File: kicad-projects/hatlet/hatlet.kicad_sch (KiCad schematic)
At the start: 40 parts, among them J1 USB Header, J2 SWD, J3 PMOD0, J4 PMOD2, J5 PMOD1, SW1 BOOTSEL, U1 AMS1117-3.3, U2 RP2040, U3 W25Q128JVS, Y1 Crystal 12MHz

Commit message: Finish rev A schematic
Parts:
- added D3: USB, LED_SMD:LED_0201_0603Metric, symbol Device:LED_Small
- added D4: 3V3, LED_SMD:LED_0201_0603Metric, symbol Device:LED_Small
- added J6: UART0, Connector_PinHeader_2.54mm:PinHeader_1x03_P2.54mm_Vertical, symbol Connector:Conn_01x03_Pin
- added J7: PMOD3, pmod:PMOD_PinSocket_2x06_P2.54mm_Horizontal, symbol pmod:PMOD_Host_Conn_02x06
- added R8, R9: 1k, Resistor_SMD:R_0603_1608Metric, symbol Device:R_Small
- SW1: lcsc (none) -> https://www.lcsc.com/product-detail/Tactile-Switches_G-Swit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
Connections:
- net +3V3: now also D4.2 (A), J7.12 (VCC), J7.6 (VCC); no longer U1.2 (VO)
- net GND: now also J1.1 (A0), J1.2 (A1), J1.7 (B0), J1.8 (B1), J6.3 (Pin_3), J7.11 (GND), J7.5 (GND), R8.2, R9.2
- net I2C0_SCL: now also J3.3 (A2); no longer J3.4 (A3)
- net I2C0_SDA: now also J3.4 (A3); no longer J3.3 (A2)
- net I2C1_SCL: now also J3.9 (B2); no longer J3.10 (B3)
- net I2C1_SDA: now also J3.10 (B3); no longer J3.9 (B2)
- net VBUS: now also D3.2 (A)
- net UART0_RX: now reaches J4.9 (B2)
- net UART0_RX: now also U2.28 (GPIO17), J6.2 (Pin_2)
- net UART0_TX: now reaches U2.27 (GPIO16)
- net UART0_TX: now also J4.8 (B1), J6.1 (Pin_1)
- net GPIO24: now reaches U2.36 (GPIO24)
- net GPIO24: now also J7.3 (A2)
- net GPIO25: now reaches U2.37 (GPIO25)
- net GPIO25: now also J7.4 (A3)
- net GPIO26: now reaches U2.38 (GPIO26_ADC0)
- net GPIO26: now also J7.7 (B0)
- net GPIO27: now reaches U2.39 (GPIO27_ADC1)
- net GPIO27: now also J7.8 (B1)
- net GPIO28: now reaches U2.40 (GPIO28_ADC2)
- net GPIO28: now also J7.9 (B2)
- net GPIO29: now reaches U2.41 (GPIO29_ADC3)
- net GPIO29: now also J7.10 (B3)
- net QSPI_CS renamed QSPI_CSn
- net SPI0_INT: no longer names the net of J4.7 (B0)
- net SPI0_INT: no longer U2.34 (GPIO22)
- net SPI0_RESET renamed GPIO23
- net GPIO23: now also J7.2 (A1); no longer J4.8 (B1)
- new net: D3.1 (K), R8.1
- new net: D4.1 (K), R9.1
- new net GPIO22: J7.1 (A0), U2.34 (GPIO22)
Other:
- note added: "-- top row (SPI0) -- 1 SPI0 ~{CS} (GPIO21) 2 SPI0 MOSI (GPIO19) 3 SPI0 MISO (GPIO20) 4 SPI0 SCK (GPIO18) 5 GND 6 VCC -- bottom row (UART0) -- 7 NC 8 UART0 TX (Host -> PMOD) (GPIO16) 9 UART0 RX (Host <- PMOD) (GPIO17) 10 NC 11 GND 12 VCC"
- note added: "-- top row -- 1 GPIO22 2 GPIO23 3 GPIO24 4 GPIO25 5 GND 6 VCC -- bottom row -- 7 GPIO26 8 GPIO27 9 GPIO28 10 GPIO29 11 GND 12 VCC"
- note added: "-- top row -- 1 I2C0 ~{INT} (GPIO2) 2 I2C0 RESET (GPIO3) 3 I2C0 SCL (GPIO5) 4 I2C0 SDA (GPIO4) 5 GND 6 VCC -- bottom row -- 7 I2C1 ~{INT} (GPIO6) 8 I2C1 RESET (GPIO7) 9 I2C1 SCL (GPIO9) 10 I2C1 SDA (GPIO8) 11 GND 12 VCC"
- note added: "-- top row -- 1 SPI1 ~{CS} (GPIO13) 2 SPI1 MOSI (GPIO11) 3 SPI1 MISO (GPIO12) 4 SPI1 SCK (GPIO10) 5 GND 6 VCC -- bottom row -- 7 SPI0 INT (GPIO14) 8 SPI0 RESET (GPIO15) 9 NC 10 NC 11 GND 12 VCC"
- note added: "PMOD1 Pinout (Extended SPI)"
- note added: "PMOD2 Pinout (SPI/UART)"
- note added: "PMOD3 Pinout (GPIO)"
- note added: "Pads for UART header"
- note added: "Power Indicators"
- note added: "SWD rescue port"
- note added: "The RP2040 peripherals can be routed pretty freely across the availble IO. However, when assigning them to PMOD sockets, the pin order of the RP2040 pin mux and the PMOD connector generally don't match."
- note removed: "-- top row -- 1 I2C0 ~{INT} (GPIO2) 2 I2C0 RESET (GPIO3) 3 I2C0 SCL (GPIO4) 4 I2C0 SDA (GPIO5) 5 GND 6 VCC -- bottom row -- 7 I2C1 ~{INT} (GPIO6) 8 I2C1 RESET (GPIO7) 9 I2C1 SCL (GPIO8) 10 I2C1 SDA (GPIO9) 11 GND 12 VCC"
- note removed: "-- top row -- 1 SPI1 ~{CS} (GPIO13) 2 SPI1 MOSI (GPIO11) 3 SPI1 MISO (GPIO12) 4 SPI1 SCK (GPIO10) 5 GND 6 VCC -- bottom row -- 7 SPI0 INT (GPIO14) 8 SPI0 RESET (GPIO15) 9 N/S 10 N/S 11 GND 12 VCC"
- note removed: "Good to have: - LEDs! - SPI PMOD - I2C PMOD - UART PMOD"
- note removed: "PMOD1 Pinout (SPI)"
- note removed: "PMOD2 Pinout (SPI)"
- moved on the sheet: C12, C13, D1, D2, J2, J3, J4, R6, R7, U1

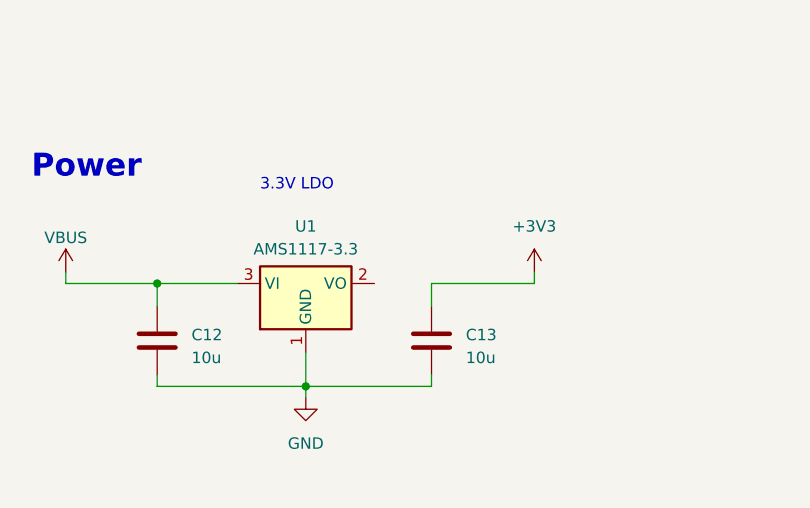
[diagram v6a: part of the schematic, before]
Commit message: Start rev A layout
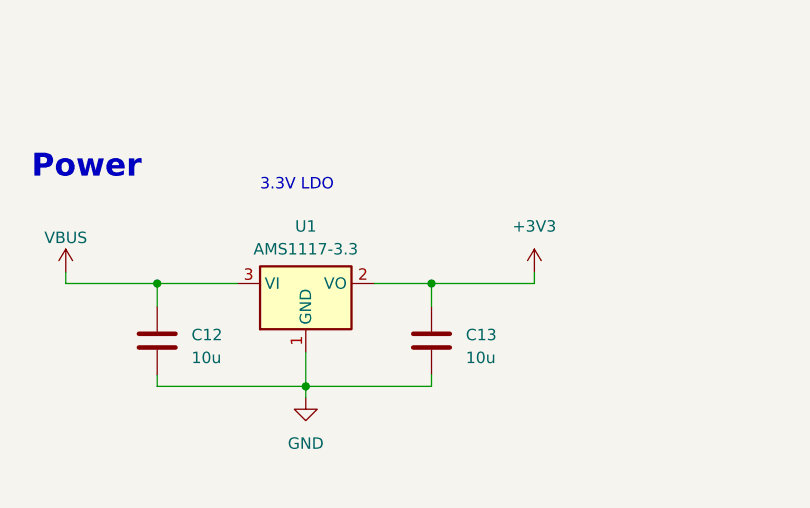
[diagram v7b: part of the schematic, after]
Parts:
- C14, C15, C16: footprint Capacitor_SMD:C_0201_0603Metric -> Capacitor_SMD:C_0603_1608Metric
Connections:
- net +3V3: now also U1.2 (VO)
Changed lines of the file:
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@@
   (junction (at 63.5 209.55) (diameter 0) (color 0 0 0 0)
   )
+  (junction (at 210.82 261.62) (diameter 0) (color 0 0 0 0)
+  )
   (junction (at 71.12 271.78) (diameter 0) (color 0 0 0 0)
   )
@@
     (stroke (width 0) (type default))
   )
+  (wire (pts (xy 204.47 261.62) (xy 210.82 261.62))
+    (stroke (width 0) (type default))
+  )
   (wire (pts (xy 80.01 264.16) (xy 80.01 265.43))
     (stroke (width 0) (type default))
@@
       (effects (font (size 1.27 1.27)) (justify right))
     )
-    (property "Footprint" "Capacitor_SMD:C_0201_0603Metric" (at 36.83 87.63 0)
+    (property "Footprint" "Capacitor_SMD:C_0603_1608Metric" (at 36.83 87.63 0)
       (effects (font (size 1.27 1.27)) hide)
     )
@@
       (effects (font (size 1.27 1.27)) (justify right))
     )
-    (property "Footprint" "Capacitor_SMD:C_0201_0603Metric" (at 60.96 267.97 0)
+    (property "Footprint" "Capacitor_SMD:C_0603_1608Metric" (at 60.96 267.97 0)
       (effects (font (size 1.27 1.27)) hide)
     )
@@
       (effects (font (size 1.27 1.27)) (justify right))
     )
-    (property "Footprint" "Capacitor_SMD:C_0201_0603Metric" (at 80.01 267.97 0)
+    (property "Footprint" "Capacitor_SMD:C_0603_1608Metric" (at 80.01 267.97 0)
       (effects (font (size 1.27 1.27)) hide)
     )

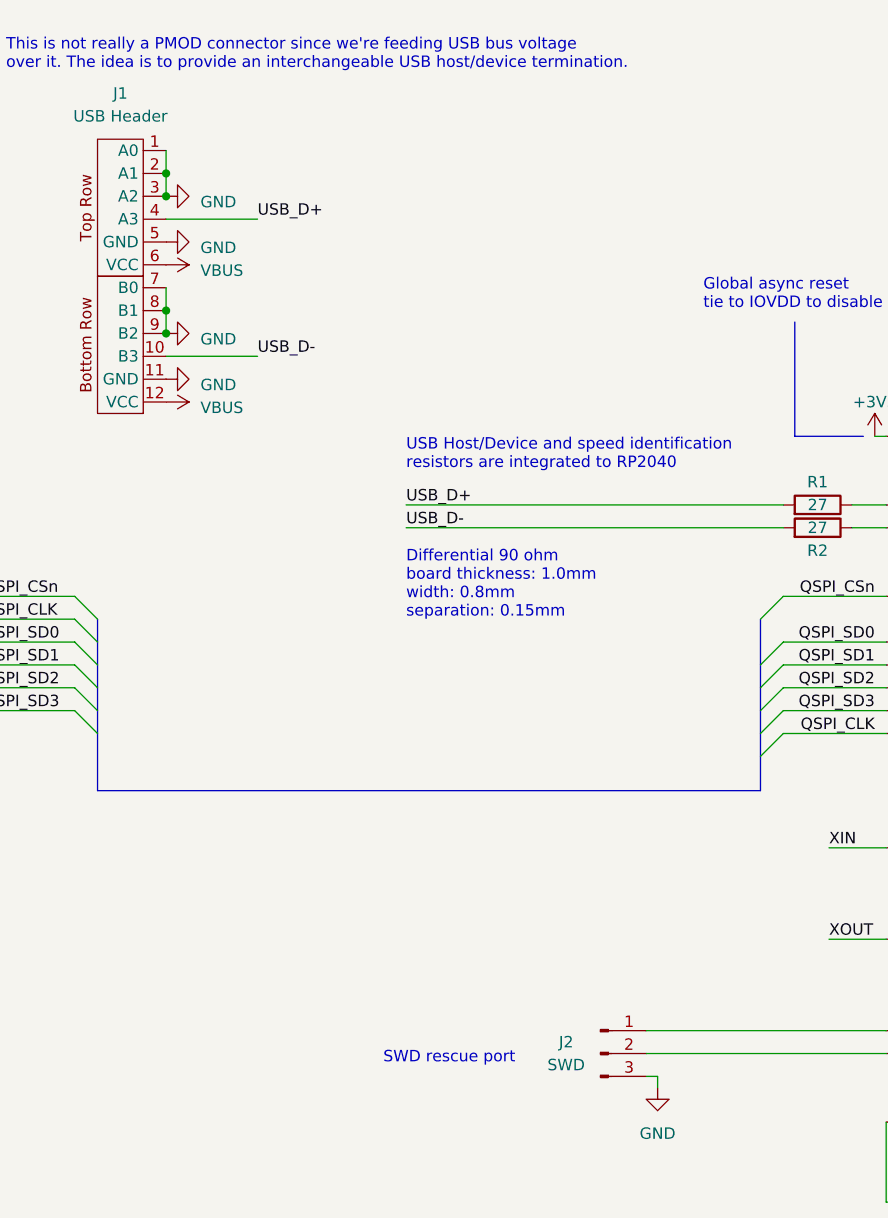
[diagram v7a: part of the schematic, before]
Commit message: WIP: lay out USB, crystal, decoupling
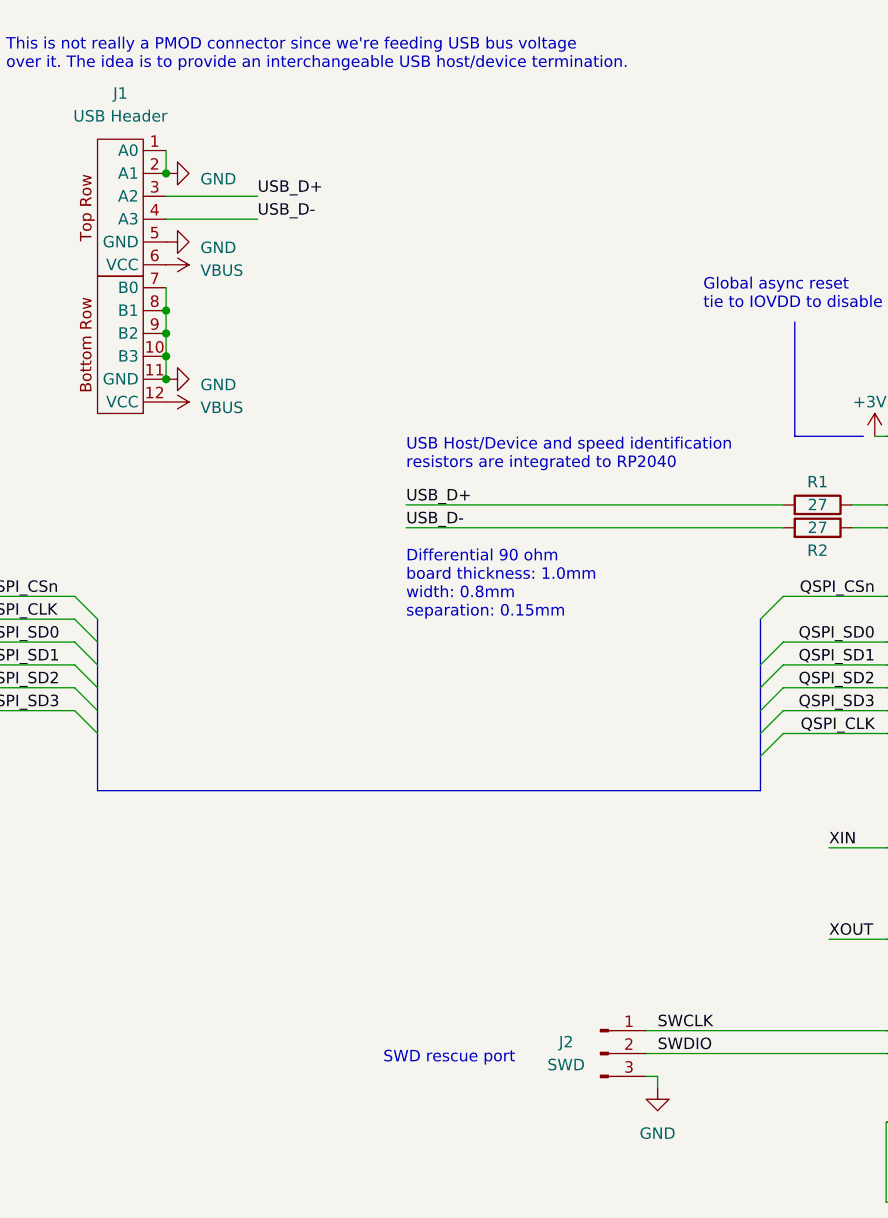
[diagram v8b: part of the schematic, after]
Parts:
- D1, D2, D3, D4: footprint LED_SMD:LED_0201_0603Metric -> LED_SMD:LED_0603_1608Metric
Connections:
- net GND: now also J1.10 (B3); no longer J1.3 (A2)
- net USB_D+: now also J1.3 (A2); no longer J1.4 (A3)
- net USB_D-: now also J1.4 (A3); no longer J1.10 (B3)
- net SWCLK: now reaches J2.1 (Pin_1), U2.24 (SWCLK)
- net SWDIO: now reaches J2.2 (Pin_2), U2.25 (SWD)
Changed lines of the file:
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@@
     (comment 1 "Authors: Verneri Hirvonen (2023)")
   )
-  (junction (at 81.28 46.99) (diameter 0) (color 0 0 0 0)
-  )
   (junction (at 83.82 201.93) (diameter 0) (color 0 0 0 0)
   )
@@
   (junction (at 53.34 219.71) (diameter 0) (color 0 0 0 0)
   )
+  (junction (at 81.28 46.99) (diameter 0) (color 0 0 0 0)
+  )
   (junction (at 73.66 209.55) (diameter 0) (color 0 0 0 0)
   )
@@
   (junction (at 265.43 273.05) (diameter 0) (color 0 0 0 0)
   )
+  (junction (at 81.28 64.77) (diameter 0) (color 0 0 0 0)
+  )
   (junction (at 276.86 142.24) (diameter 0) (color 0 0 0 0)
   )
@@
   (junction (at 275.59 273.05) (diameter 0) (color 0 0 0 0)
   )
+  (junction (at 81.28 67.31) (diameter 0) (color 0 0 0 0)
+  )
   (junction (at 63.5 209.55) (diameter 0) (color 0 0 0 0)
   )
@@
   (junction (at 119.38 264.16) (diameter 0) (color 0 0 0 0)
   )
-  (junction (at 237.49 105.41) (diameter 0) (color 0 0 0 0)
-  )
   (junction (at 81.28 62.23) (diameter 0) (color 0 0 0 0)
   )
-  (junction (at 81.28 49.53) (diameter 0) (color 0 0 0 0)
+  (junction (at 237.49 105.41) (diameter 0) (color 0 0 0 0)
   )
   (junction (at 53.34 201.93) (diameter 0) (color 0 0 0 0)
@@
   (junction (at 194.31 66.04) (diameter 0) (color 0 0 0 0)
   )
-  (junction (at 81.28 64.77) (diameter 0) (color 0 0 0 0)
+  (junction (at 81.28 69.85) (diameter 0) (color 0 0 0 0)
   )
   (junction (at 80.01 264.16) (diameter 0) (color 0 0 0 0)
@@
     (stroke (width 0) (type default))
   )
+  (wire (pts (xy 81.28 62.23) (xy 81.28 64.77))
+    (stroke (width 0) (type default))
+  )
   (wire (pts (xy 59.69 106.68) (xy 71.12 106.68))
     (stroke (width 0) (type default))
@@
     (stroke (width 0) (type default))
   )
-  (wire (pts (xy 81.28 44.45) (xy 81.28 46.99))
-    (stroke (width 0) (type default))
-  )
   (wire (pts (xy 212.09 76.2) (xy 218.44 76.2))
     (stroke (width 0) (type default))
@@
     (stroke (width 0) (type default))
   )
-  (wire (pts (xy 81.28 62.23) (xy 81.28 64.77))
-    (stroke (width 0) (type default))
-  )
   (wire (pts (xy 212.09 106.68) (xy 234.95 106.68))
     (stroke (width 0) (type default))
@@
     (stroke (width 0) (type default))
   )
-  (wire (pts (xy 81.28 59.69) (xy 81.28 62.23))
-    (stroke (width 0) (type default))
-  )
   (bus (pts (xy 270.51 88.9) (xy 300.99 88.9))
     (stroke (width 0) (type default))
@@
     (stroke (width 0) (type default))
   )
+  (wire (pts (xy 81.28 64.77) (xy 81.28 67.31))
+    (stroke (width 0) (type default))
+  )
   (wire (pts (xy 186.69 161.29) (xy 161.29 161.29))
     (stroke (width 0) (type default))
@@
     (stroke (width 0) (type default))
   )
+  (wire (pts (xy 81.28 44.45) (xy 81.28 46.99))
+    (stroke (width 0) (type default))
+  )
   (wire (pts (xy 83.82 201.93) (xy 83.82 203.2))
     (stroke (width 0) (type default))
@@
     (stroke (width 0) (type default))
   )
+  (wire (pts (xy 81.28 67.31) (xy 81.28 69.85))
+    (stroke (width 0) (type default))
+  )
   (bus (pts (xy 237.49 147.32) (xy 237.49 149.86))
     (stroke (width 0) (type default))
@@
     (stroke (width 0) (type default))
   )
-  (wire (pts (xy 81.28 46.99) (xy 81.28 49.53))
-    (stroke (width 0) (type default))
-  )
   (wire (pts (xy 44.45 208.28) (xy 44.45 209.55))
     (stroke (width 0) (type default))
@@
     (stroke (width 0) (type default))
   )
+  (wire (pts (xy 81.28 59.69) (xy 81.28 62.23))
+    (stroke (width 0) (type default))
+  )
   (bus (pts (xy 237.49 139.7) (xy 237.49 142.24))
     (stroke (width 0) (type default))
@@
     (stroke (width 0) (type default))
   )
-  (wire (pts (xy 91.44 67.31) (xy 81.28 67.31))
+  (wire (pts (xy 91.44 49.53) (xy 81.28 49.53))
     (stroke (width 0) (type default))
   )
@@
     (effects (font (size 1.27 1.27)) (justify left bottom))
   )
+  (label "SWCLK" (at 135.89 142.24 0) (fields_autoplaced)
+    (effects (font (size 1.27 1.27)) (justify left bottom))
+  )
   (label "QSPI_CLK" (at 160.02 109.22 180) (fields_autoplaced)
     (effects (font (size 1.27 1.27)) (justify right bottom))
@@
     (effects (font (size 1.27 1.27)) (justify left bottom))
   )
+  (label "SWDIO" (at 135.89 144.78 0) (fields_autoplaced)
+    (effects (font (size 1.27 1.27)) (justify left bottom))
+  )
   (label "LED0" (at 21.59 242.57 180) (fields_autoplaced)
     (effects (font (size 1.27 1.27)) (justify right bottom))
@@
     (effects (font (size 1.27 1.27)) (justify right bottom))
   )
-  (label "USB_D+" (at 91.44 52.07 0) (fields_autoplaced)
+  (label "USB_D+" (at 91.44 49.53 0) (fields_autoplaced)
     (effects (font (size 1.27 1.27)) (justify left bottom))
   )
@@
     (effects (font (size 1.27 1.27)) (justify left bottom))
   )
-  (label "USB_D-" (at 91.44 67.31 0) (fields_autoplaced)
+  (label "USB_D-" (at 91.44 52.07 0) (fields_autoplaced)
     (effects (font (size 1.27 1.27)) (justify left bottom))
   )
@@
     )
   )
-  (symbol (lib_name "GND_3") (lib_id "power:GND") (at 81.28 64.77 90) (unit 1)
-    (in_bom yes) (on_board yes) (dnp no) (fields_autoplaced)
-    (property "Reference" "#PWR015" (at 87.63 64.77 0)
-      (effects (font (size 1.27 1.27)) hide)
-    )
-    (property "Value" "GND" (at 85.09 65.405 90)
-      (effects (font (size 1.27 1.27)) (justify right))
-    )
-    (property "Footprint" "" (at 81.28 64.77 0)
-      (effects (font (size 1.27 1.27)) hide)
-    )
-    (property "Datasheet" "" (at 81.28 64.77 0)
-      (effects (font (size 1.27 1.27)) hide)
-    )
-    (pin "1")
-    (instances
-      (project "hatlet"
-        (path "/422c1aa7-bd8c-4c94-9e5b-2fd049d9e649"
-          (reference "#PWR015") (unit 1)
-        )
-      )
-    )
-  )
   (symbol (lib_id "Connector:Conn_01x03_Pin") (at 129.54 144.78 0) (unit 1)
     (in_bom yes) (on_board yes) (dnp no)
@@
     )
   )
+  (symbol (lib_name "GND_3") (lib_id "power:GND") (at 81.28 46.99 90) (unit 1)
+    (in_bom yes) (on_board yes) (dnp no) (fields_autoplaced)
+    (property "Reference" "#PWR014" (at 87.63 46.99 0)
+      (effects (font (size 1.27 1.27)) hide)
+    )
+    (property "Value" "GND" (at 85.09 47.625 90)
+      (effects (font (size 1.27 1.27)) (justify right))
+    )
+    (property "Footprint" "" (at 81.28 46.99 0)
+      (effects (font (size 1.27 1.27)) hide)
+    )
+    (property "Datasheet" "" (at 81.28 46.99 0)
+      (effects (font (size 1.27 1.27)) hide)
+    )
+    (pin "1")
+    (instances
+      (project "hatlet"
+        (path "/422c1aa7-bd8c-4c94-9e5b-2fd049d9e649"
+          (reference "#PWR014") (unit 1)
+        )
+      )
+    )
+  )
   (symbol (lib_name "GND_3") (lib_id "power:GND") (at 81.28 54.61 90) (unit 1)
     (in_bom yes) (on_board yes) (dnp no) (fields_autoplaced)
@@
       (effects (font (size 1.27 1.27)) (justify right))
     )
-    (property "Footprint" "LED_SMD:LED_0201_0603Metric" (at 36.83 245.11 90)
+    (property "Footprint" "LED_SMD:LED_0603_1608Metric" (at 36.83 245.11 90)
       (effects (font (size 1.27 1.27)) hide)
     )
@@
       (effects (font (size 1.27 1.27)) (justify right))
     )
-    (property "Footprint" "LED_SMD:LED_0201_0603Metric" (at 21.59 270.51 90)
+    (property "Footprint" "LED_SMD:LED_0603_1608Metric" (at 21.59 270.51 90)
       (effects (font (size 1.27 1.27)) hide)
     )
@@
       (effects (font (size 1.27 1.27)) (justify right))
     )
-    (property "Footprint" "LED_SMD:LED_0201_0603Metric" (at 21.59 245.11 90)
+    (property "Footprint" "LED_SMD:LED_0603_1608Metric" (at 21.59 245.11 90)
       (effects (font (size 1.27 1.27)) hide)
     )
@@
       (effects (font (size 1.27 1.27)) (justify right))
     )
-    (property "Footprint" "LED_SMD:LED_0201_0603Metric" (at 36.83 270.51 90)
+    (property "Footprint" "LED_SMD:LED_0603_1608Metric" (at 36.83 270.51 90)
       (effects (font (size 1.27 1.27)) hide)
     )
@@
         )
       )
-    )
-  )
-  (symbol (lib_name "GND_3") (lib_id "power:GND") (at 81.28 49.53 90) (unit 1)
-    (in_bom yes) (on_board yes) (dnp no) (fields_autoplaced)
-    (property "Reference" "#PWR014" (at 87.63 49.53 0)
-      (effects (font (size 1.27 1.27)) hide)
-    )
-    (property "Value" "GND" (at 85.09 50.165 90)
-      (effects (font (size 1.27 1.27)) (justify right))
-    )
-    (property "Footprint" "" (at 81.28 49.53 0)
-      (effects (font (size 1.27 1.27)) hide)
-    )
-    (property "Datasheet" "" (at 81.28 49.53 0)
-      (effects (font (size 1.27 1.27)) hide)
-    )
-    (pin "1")
-    (instances
-      (project "hatlet"
-        (path "/422c1aa7-bd8c-4c94-9e5b-2fd049d9e649"
-          (reference "#PWR014") (unit 1)
-        )
-      )
